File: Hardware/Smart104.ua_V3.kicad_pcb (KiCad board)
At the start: 4 copper layers, 104 x 54.5 mm, 162 parts, among them J1 KLS1-207-1-04-S, J2 KLS1-207-1-04-S, J3 KLS1-207-1-05-S, J4 KLS2-308V-2.54-02P-4S, J5 SIM8051-6-0-14-00-A, J6 KLS2-308V-2.54-03P-4S, J7 KLS1-207-1-04-S, J8 KLS1-207-1-02-S, J9 1909763-1, Q1 BC847CW,115, Q2 AO3419, Q3 BC847CW,115, Q4 BC847CW,115, Q5 BC847CW,115, Q6 AO3419, Q7 BC847CW,115, U1 BC66NADA-04-STD, U2 TXS0108EPW, U3 TPS63900, U4 AT25SF321B-SSHB-T, U5 MIC5504-3.3YM5, U6 EFM32TG11B320F128GQ64-B, U7 LIS3DH, U8 Si7055-A20, Y1 32.768kHz, Y2 ABM8-48-000MHZ

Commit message: new: Rev. 1.0 gerbers/fixes_2
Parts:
- moved C14 0.60 mm to (184.0, 100.8)
- moved C16 0.60 mm to (180.6, 100.8)
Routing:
- net GND: track 219.1 -> 208.8 mm, vias 223 -> 222
- net SDO: track 3.32 -> 4.10 mm
- net SIM_CLK: track 4.79 -> 5.50 mm
- net +3V3: track 169.1 -> 169.8 mm
- net SIM_RST: track 6.09 -> 6.65 mm
- net BC66_RI: track 5.63 -> 6.15 mm

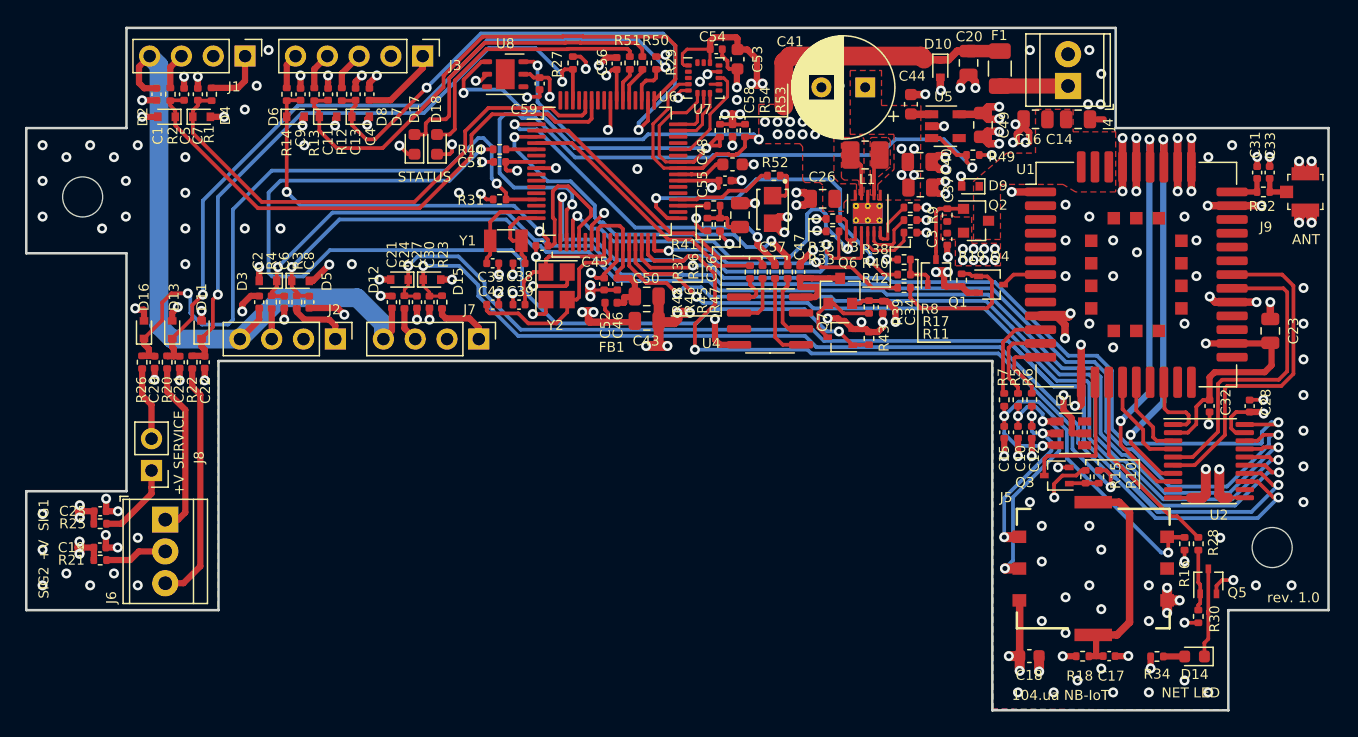
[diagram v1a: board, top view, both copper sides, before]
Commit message: fix: Rev. 1.0 connector added, pcb fixes
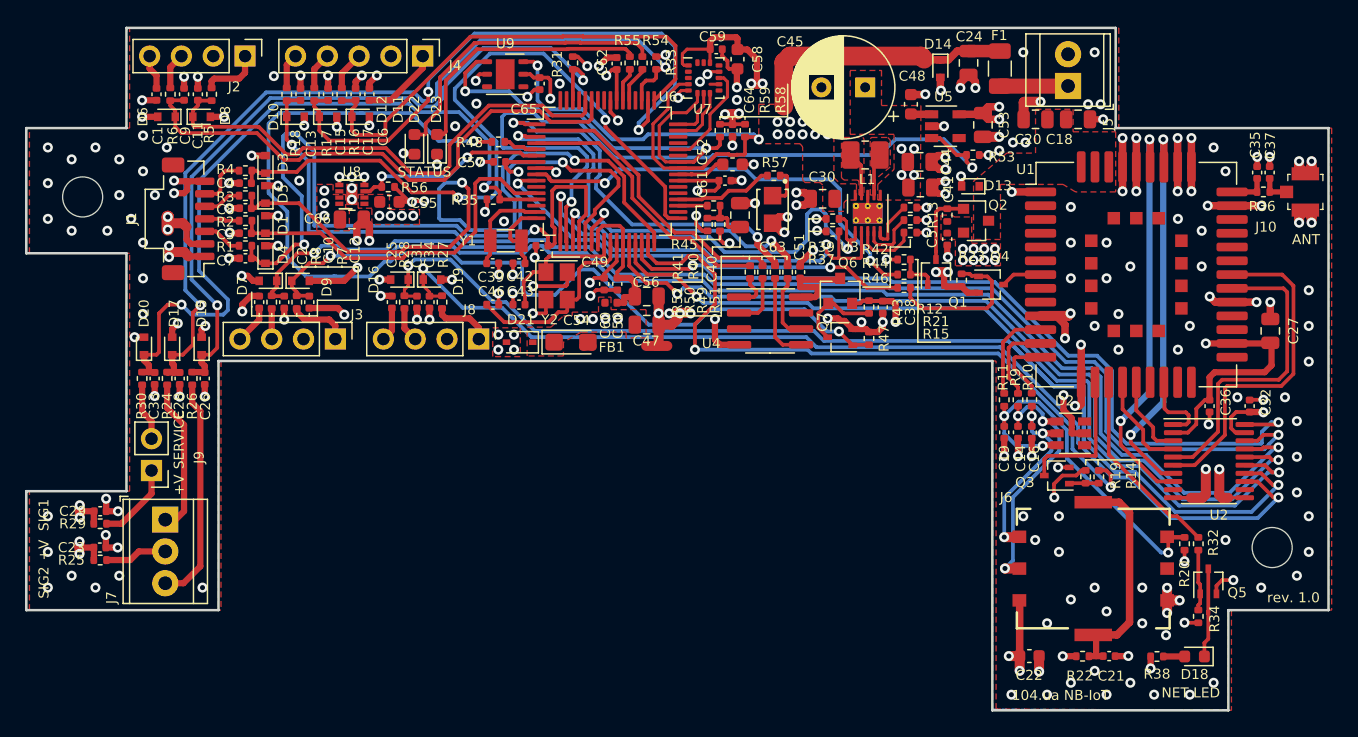
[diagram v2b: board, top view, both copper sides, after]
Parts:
- removed the C19 at (105.9, 135.0)
- removed the R21 at (105.9, 136.0)
- added C23: 0.1uF, Capacitor_SMD:C_0402_1005Metric, F.Cu at (105.9, 135.0)
- added C3: 18pF, Capacitor_SMD:C_0402_1005Metric, F.Cu at (117.5, 109.9)
- added C4: 18pF, Capacitor_SMD:C_0402_1005Metric, F.Cu at (117.5, 105.9)
- added C54: 100uF, Capacitor_Tantalum_SMD:CP_EIA-3216-18_Kemet-A, F.Cu at (143.5, 118.6)
- added C55: 1uF, Capacitor_SMD:C_0603_1608Metric, F.Cu at (129.0, 107.4)
- added C66: 10uF, Capacitor_SMD:C_0805_2012Metric, F.Cu at (126.0, 108.8)
- added C7: 18pF, Capacitor_SMD:C_0402_1005Metric, F.Cu at (117.5, 111.9)
- added C8: 18pF, Capacitor_SMD:C_0402_1005Metric, F.Cu at (117.5, 107.9)
- added D1: PESD5V0L1UB,115, Diode_SMD:D_SOD-523, F.Cu at (119.1, 109.2)
- added D21: BAT46JFILM, Diode_SMD:D_SOD-323, F.Cu at (139.4, 118.6)
- added D3: PESD5V0L1UB,115, Diode_SMD:D_SOD-523, F.Cu at (119.1, 104.4)
- added D4: PESD5V0L1UB,115, Diode_SMD:D_SOD-523, F.Cu at (119.1, 111.6)
- added D5: PESD5V0L1UB,115, Diode_SMD:D_SOD-523, F.Cu at (119.1, 106.8)
- added J1: 5013310707, Connector_Molex:Molex_Pico-Clasp_501331-0707_1x07-1MP_P1.00mm_Vertical, F.Cu at (112.9, 108.8)
- added R1: 22R, Resistor_SMD:R_0402_1005Metric, F.Cu at (117.5, 110.9)
- added R2: 22R, Resistor_SMD:R_0402_1005Metric, F.Cu at (117.5, 108.9)
- added R25: 470R, Resistor_SMD:R_0402_1005Metric, F.Cu at (105.9, 136.0)
- added R3: 22R, Resistor_SMD:R_0402_1005Metric, F.Cu at (117.5, 106.9)
- added R4: 22R, Resistor_SMD:R_0402_1005Metric, F.Cu at (117.5, 104.9)
- added R56: 10K, Resistor_SMD:R_0402_1005Metric, F.Cu at (128.9, 106.2)
- added U8: MCP1727-3302E_MF, Package_DFN_QFN:VDFN-8-1EP_2x2mm_P0.5mm_EP0.9x1.7mm, F.Cu at (126.0, 106.8)
- C45: renamed from C41; value 820uF -> 1000uF
- moved D15 1.30 mm to (114.0, 118.9)
- moved D17 1.30 mm to (111.7, 118.9)
- moved D20 1.30 mm to (109.4, 118.9)
- moved C26 1.30 mm to (114.2, 121.5)
- moved C28 1.30 mm to (112.2, 121.5)
- moved C33 1.30 mm to (110.2, 121.5)
- moved R24 1.30 mm to (111.2, 121.5)
- moved R26 1.30 mm to (113.2, 121.5)
- moved R30 1.30 mm to (109.2, 121.5)
- moved R48 0.61 mm to (137.7, 102.6)
- moved R35 0.50 mm to (137.3, 107.2)
- moved C56 0.30 mm to (149.6, 117.2)
- renumbered C6 to C10, C7 to C11, C8 to C12, C9 to C13, C10 to C14, C11 to C15, C12 to C16, C13 to C17, C14 to C18, C15 to C19, C16 to C20, C17 to C21, C18 to C22, C20 to C24, C21 to C25, C22 to C26, C23 to C27, C24 to C28, C25 to C29, C26 to C30, C27 to C31, C28 to C32, C29 to C33, C30 to C34, C31 to C35, C32 to C36, C33 to C37, C34 to C38, C35 to C39, C36 to C40, C37 to C41, C38 to C42, C39 to C43, C40 to C44, C42 to C46, C43 to C47, C44 to C48, C45 to C49, C3 to C5, C46 to C50, C47 to C51, C48 to C52, C49 to C53, C50 to C56, C51 to C57, C53 to C58, C54 to C59, C4 to C6, C52 to C60, C55 to C61, C56 to C62, C57 to C63, C58 to C64, C59 to C65, C5 to C9, D6 to D10, D7 to D11, D8 to D12, D9 to D13, D10 to D14, D11 to D15, D12 to D16, D13 to D17, D14 to D18, D15 to D19, D1 to D2, D16 to D20, D17 to D22, D18 to D23, D2 to D6, D3 to D7, D4 to D8, D5 to D9, J9 to J10, J1 to J2, J2 to J3, J3 to J4, J4 to J5, J5 to J6, J6 to J7, J7 to J8, J8 to J9, R6 to R10, R7 to R11, R8 to R12, R9 to R13, R10 to R14, R11 to R15, R12 to R16, R13 to R17, R14 to R18, R15 to R19, R16 to R20, R17 to R21, R18 to R22, R19 to R23, R20 to R24, R22 to R26, R23 to R27, R24 to R28, R25 to R29, R26 to R30, R27 to R31, R28 to R32, R29 to R33, R30 to R34, R31 to R35, R32 to R36, R33 to R37, R34 to R38, R35 to R39, R36 to R40, R37 to R41, R38 to R42, R39 to R43, R40 to R44, R41 to R45, R42 to R46, R43 to R47, R44 to R48, R45 to R49, R1 to R5, R46 to R50, R47 to R51, R48 to R52, R49 to R53, R50 to R54, R51 to R55, R52 to R57, R53 to R58, R54 to R59, R2 to R6, R3 to R7, R4 to R8, R5 to R9, U8 to U9
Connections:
- net VDDA renamed +3.3VADC
- C1 pad 1: VBUS -> +BATT
- C2 pad 1: VBUS -> +BATT
- C25 pad 1: VBUS -> +BATT
- C32 pad 1: +3V3 -> +BATT
- C56 pad 1: +BATT -> +3.3VP
- C57 pad 1: +BATT -> +3.3VP
- C60 pad 1: +BATT -> +3.3VP
- C61 pad 1: +BATT -> +3.3VP
- C62 pad 1: +BATT -> +3.3VP
- C64 pad 1: +3V3 -> +BATT
- F1 pad 2: VBUS -> Net-(F1-Pad2)
- FB1 pad 1: +BATT -> +3.3VP
- J2 pad 4: VBUS -> +BATT
- J3 pad 4: VBUS -> +BATT
- J5 pad 1: VBUS -> Net-(F1-Pad2)
- J8 pad 4: VBUS -> +BATT
- R58 pad 2: +3V3 -> +BATT
- R59 pad 2: +3V3 -> +BATT
- U2 pad 19: +3V3 -> +BATT
- U6 pad 10: Net-(U6-Pad10) -> BC66_PWR
- U6 pad 12: Net-(U6-Pad12) -> GPIO1
- U6 pad 21: Net-(U6-Pad21) -> GPIO0
- U6 pad 26: +BATT -> +3.3VP
- U6 pad 32: BC66_PWR -> ADC0
- U6 pad 33: BC66_ON_OFF -> ADC1
- U6 pad 39: +BATT -> +3.3VP
- U6 pad 49: MCU_SWDIO -> MCU_SWCLK
- U6 pad 50: MCU_SWCLK -> MCU_SWDIO
- U6 pad 55: +BATT -> +3.3VP
- U6 pad 6: Net-(U6-Pad6) -> SENS_ENBL
- U6 pad 7: +BATT -> +3.3VP
- U6 pad 9: Net-(U6-Pad9) -> BC66_ON_OFF
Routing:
- net VBUS: track 151.3 -> 0.00 mm
- net +3.3VP: track 0.00 -> 66.9 mm, vias 0 -> 8
- net GPIO0: track 0.00 -> 62.5 mm, vias 0 -> 2
- net ADC1: track 0.00 -> 58.4 mm, vias 0 -> 2
- net ADC0: track 0.00 -> 57.9 mm, vias 0 -> 2
- net GPIO1: track 0.00 -> 30.0 mm
- net VCCQ: track 0.00 -> 24.3 mm, vias 0 -> 5
- net GND: track 208.8 -> 227.7 mm, vias 222 -> 242
- net +3V3: track 169.8 -> 151.7 mm, vias 10 -> 7
- net SENS_ENBL: track 0.00 -> 15.6 mm, vias 0 -> 2
- net BC66_PWR: track 21.5 -> 35.4 mm
- net MCU_EM4WU5: track 52.5 -> 60.0 mm
- net BC66_ON_OFF: track 27.8 -> 35.1 mm
- net MCU_EM4WU6: track 53.2 -> 60.2 mm
- net MCU_EM4WU4: track 61.8 -> 67.8 mm
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- added copper zone on F.Cu, net +3.3VP
- added copper zone on In2.Cu, net +3.3VP
- added copper zone on F.Cu, net VCCQ

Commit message: fix: Rev. 1.0 production files added
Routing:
- net ADC0: track 57.9 -> 56.2 mm
- net GND: track 227.7 -> 227.1 mm, vias 242 -> 243
- net +3.3VP: track 66.9 -> 66.3 mm
- net Net-(Q6-Pad1): track 6.92 -> 7.54 mm
